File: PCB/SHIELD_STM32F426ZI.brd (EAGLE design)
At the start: 100 x 80 mm, 1 part, among them U1 NUCLEO-F429ZI

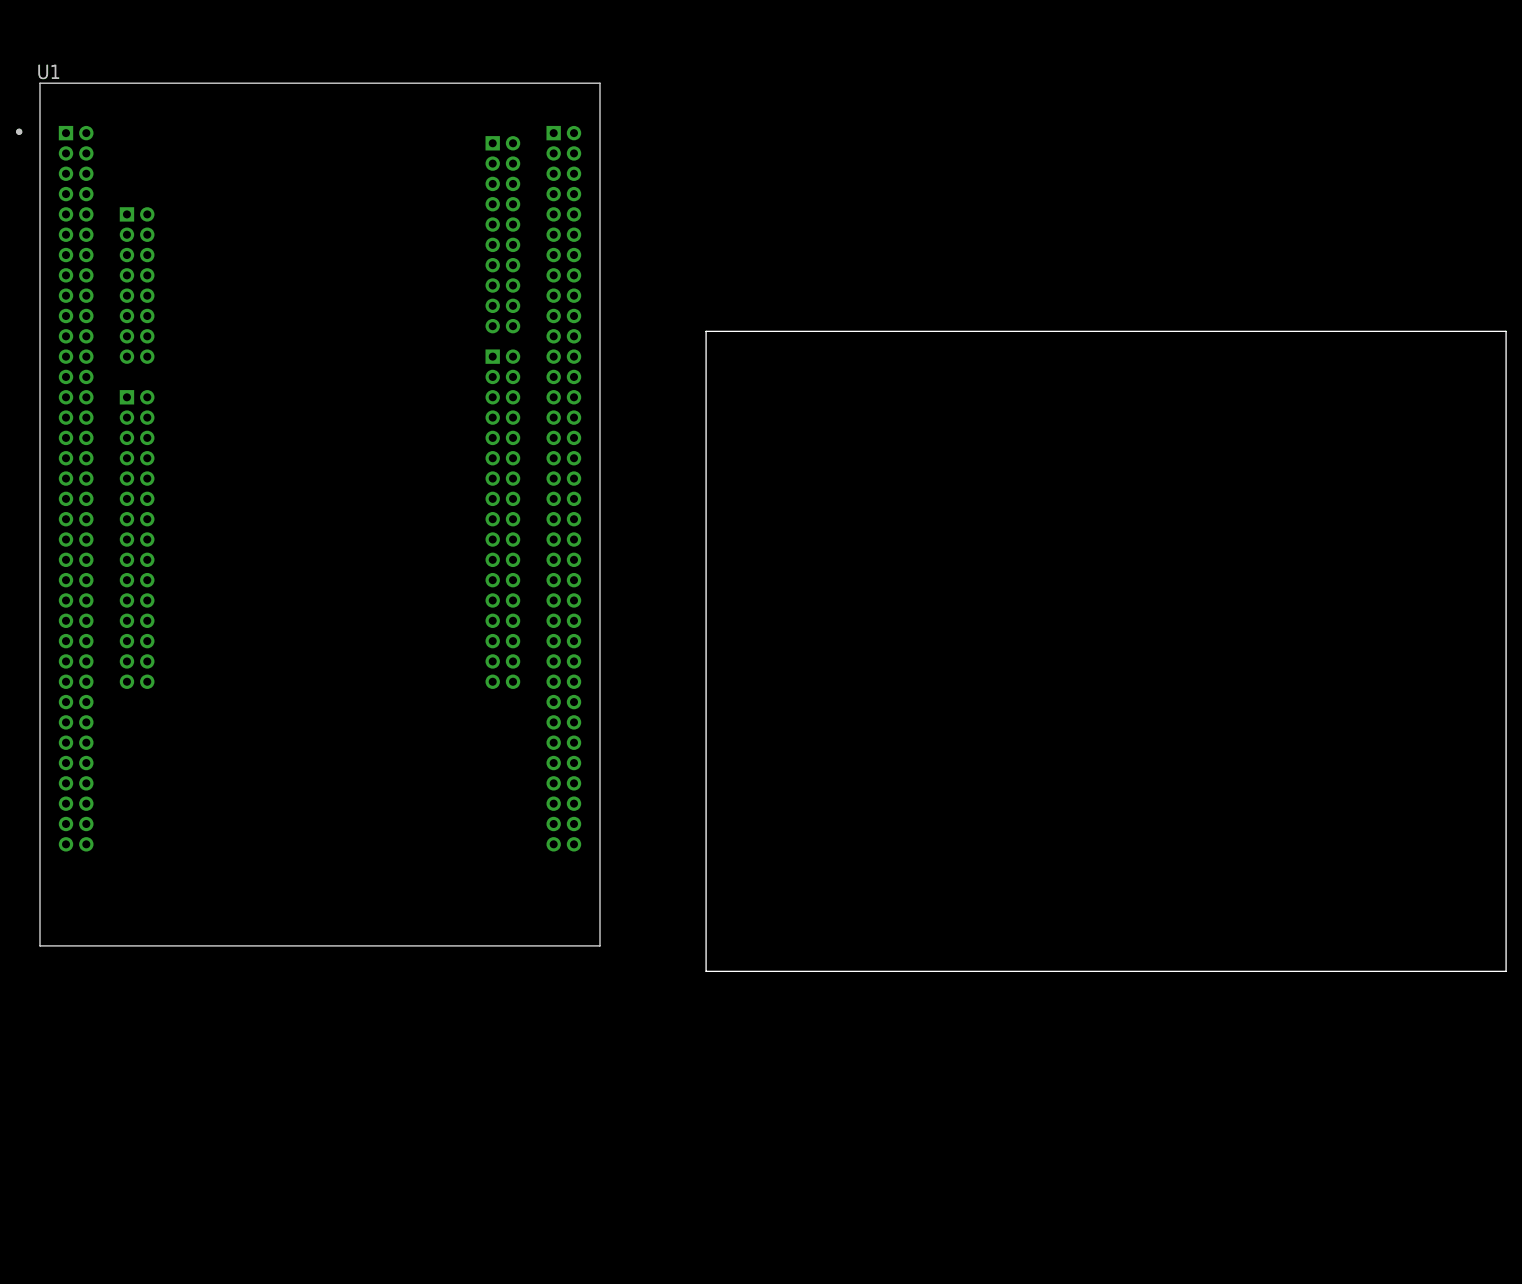
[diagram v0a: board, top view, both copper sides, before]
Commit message: new fmc pin
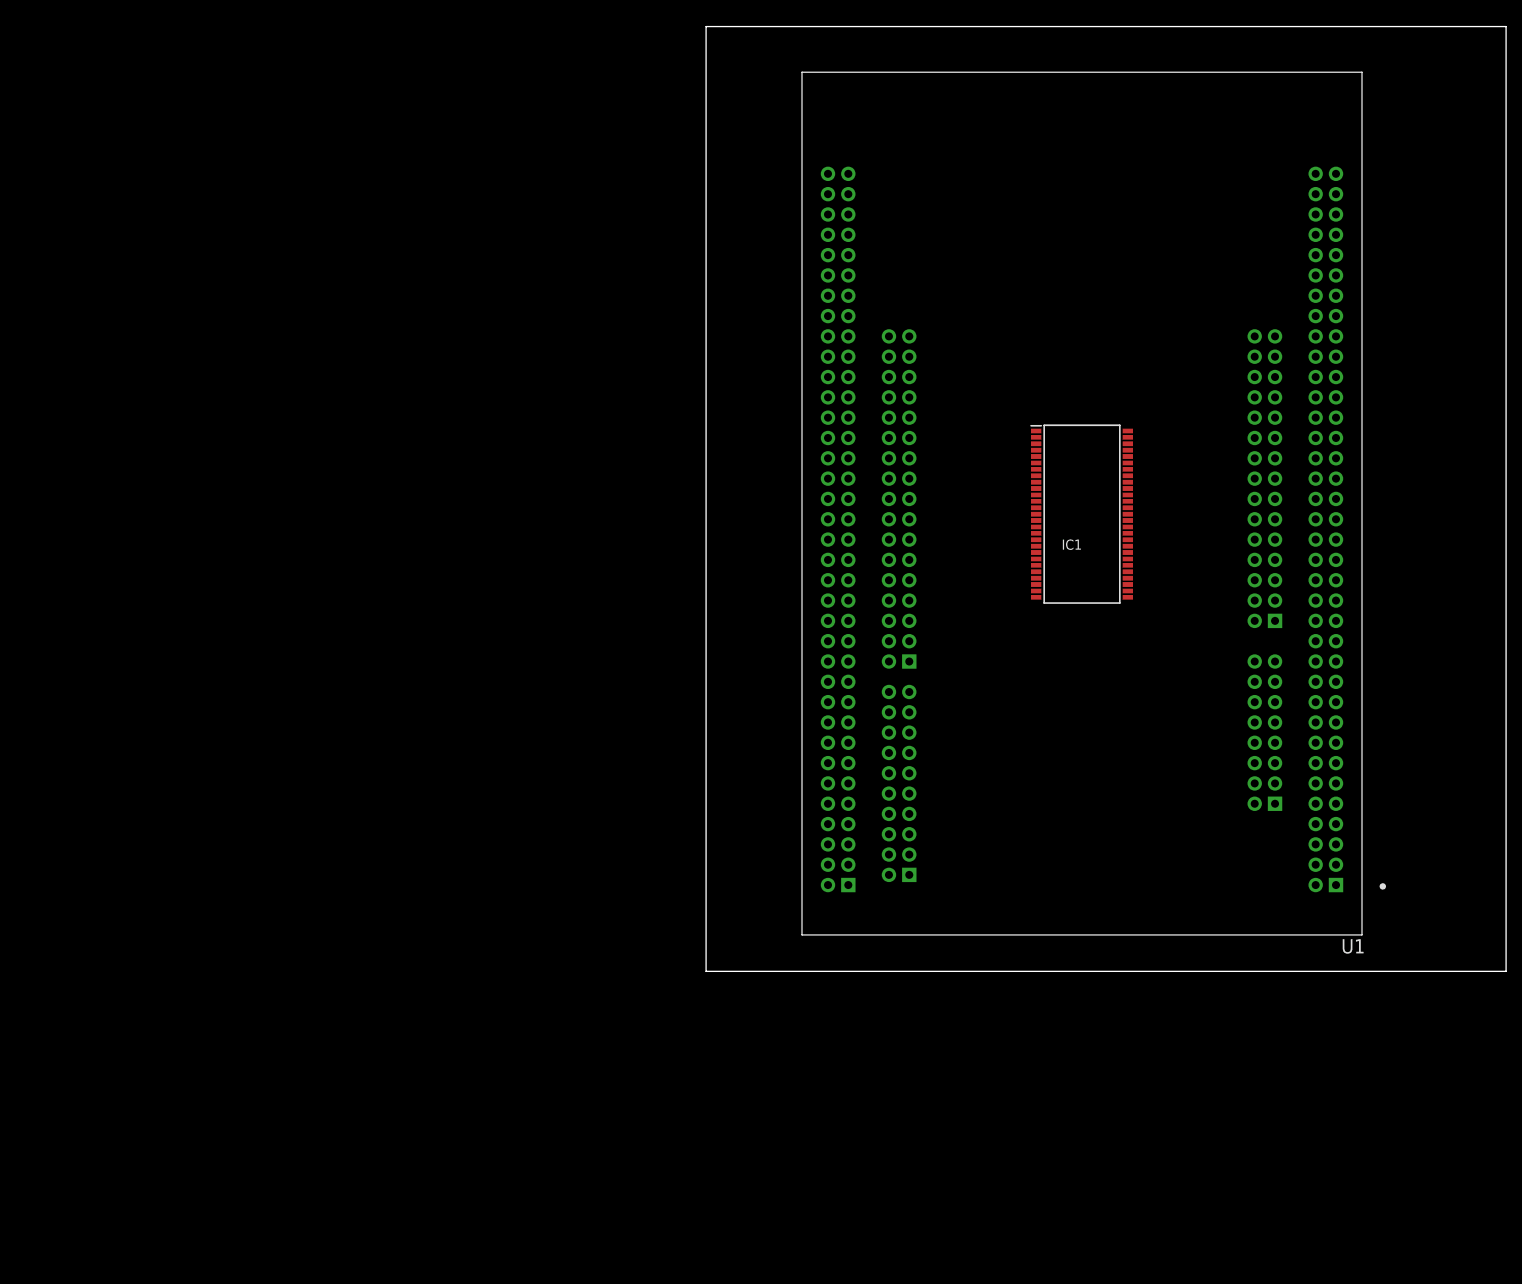
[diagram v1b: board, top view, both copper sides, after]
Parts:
- added IC1: AS4C16M16SA-6TCN, sdram:SOP80P1176X120-54N
- moved U1 95.3 mm to (47.0, 55.9), turned to 180 degrees
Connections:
- new net FMC_A0: IC1.23, U1.CN11_53
- new net FMC_A1: IC1.24, U1.CN11_51
- new net FMC_A10: IC1.22
- new net FMC_A11: IC1.35
- new net FMC_A12: IC1.36
- new net FMC_A2: IC1.25, U1.CN11_52
- new net FMC_A3: IC1.26, U1.CN12_58
- new net FMC_A4: IC1.29, U1.CN12_38
- new net FMC_A5: IC1.30, U1.CN12_36
- new net FMC_A6: IC1.31, U1.CN12_59
- new net FMC_A7: IC1.32, U1.CN12_57
- new net FMC_A8: IC1.33, U1.CN12_50
- new net FMC_A9: IC1.34, U1.CN12_60
- new net N$1: IC1.1
- new net N$10: IC1.10
- new net N$100: U1.CN11_57
- new net N$101: U1.CN11_58
- new net N$102: U1.CN11_59
- new net N$103: U1.CN11_61
- new net N$104: U1.CN11_62
- new net N$105: U1.CN11_63
- new net N$106: U1.CN11_64
- new net N$107: U1.CN11_65
- new net N$108: U1.CN11_66
- new net N$109: U1.CN11_68
- new net N$11: IC1.11
- new net N$110: U1.CN11_69
- new net N$111: U1.CN11_70
- new net N$112: U1.CN12_12
- new net N$113: U1.CN12_13
- new net N$114: U1.CN12_14
- new net N$115: U1.CN12_15
- new net N$116: U1.CN12_16
- new net N$117: U1.CN12_17
- new net N$118: U1.CN12_18
- new net N$119: U1.CN12_19
- new net N$12: IC1.12
- new net N$120: U1.CN12_21
- new net N$121: U1.CN12_22
- new net N$122: U1.CN12_23
- new net N$123: U1.CN12_24
- new net N$124: U1.CN12_25
- new net N$125: U1.CN12_26
- new net N$126: U1.CN12_27
- new net N$127: U1.CN12_28
- new net N$128: U1.CN12_29
- new net N$129: U1.CN12_30
- new net N$13: IC1.13
- new net N$130: U1.CN12_31
- new net N$131: U1.CN12_32
- new net N$132: U1.CN12_33
- new net N$133: U1.CN12_34
- new net N$134: U1.CN12_35
- new net N$136: U1.CN12_37
- new net N$138: U1.CN12_40
- new net N$139: U1.CN12_41
- new net N$14: IC1.14
- new net N$140: U1.CN12_42
- new net N$141: U1.CN12_43
- new net N$142: U1.CN12_44
- new net N$143: U1.CN12_45
- new net N$144: U1.CN12_46
- new net N$145: U1.CN12_47
- new net N$146: U1.CN12_48
- new net N$147: U1.CN12_49
- new net N$149: U1.CN12_51
- new net N$15: IC1.15
- new net N$150: U1.CN12_52
- new net N$151: U1.CN12_53
- new net N$152: U1.CN12_55
- new net N$153: U1.CN12_56
- new net N$158: U1.CN12_61
- new net N$159: U1.CN12_62
- new net N$16: IC1.16
- new net N$160: U1.CN12_64
- new net N$161: U1.CN12_65
- new net N$162: U1.CN12_66
- new net N$163: U1.CN12_67
- new net N$164: U1.CN12_68
- new net N$165: U1.CN12_69
- new net N$166: U1.CN12_70
- new net N$17: IC1.17
- new net N$18: IC1.18
- new net N$19: IC1.19
- new net N$2: IC1.2
- new net N$20: IC1.20
- new net N$21: IC1.21
- new net N$22: U1.CN12_1
- new net N$23: U1.CN11_1
- new net N$24: U1.CN11_2
- new net N$25: U1.CN11_3
- new net N$26: IC1.27
- new net N$27: IC1.54
- new net N$28: IC1.53
- new net N$29: IC1.52
- new net N$3: IC1.3
- new net N$30: IC1.51
- new net N$31: IC1.50
- new net N$32: IC1.49
- new net N$33: IC1.48
- new net N$34: IC1.47
- new net N$35: IC1.46
- new net N$36: IC1.45
- new net N$37: IC1.44
- new net N$38: IC1.43
- new net N$39: IC1.42
- new net N$4: IC1.4
- new net N$40: IC1.41
- new net N$41: IC1.40
- new net N$42: IC1.39
- new net N$43: IC1.38
- new net N$44: IC1.37
- new net N$45: U1.CN12_2
- new net N$46: U1.CN12_3
- new net N$47: U1.CN12_4
- new net N$48: U1.CN12_5
- new net N$49: U1.CN12_6
- new net N$5: IC1.5
- new net N$50: U1.CN12_7
- new net N$51: U1.CN12_8
- new net N$52: U1.CN12_20, U1.CN12_39, U1.CN12_54, U1.CN12_63, U1.CN12_71, U1.CN12_72, U1.CN12_9
- new net N$53: IC1.28
- new net N$54: U1.CN11_4
- new net N$55: U1.CN11_5
- new net N$56: U1.CN11_6
- new net N$57: U1.CN11_7
- new net N$58: U1.CN11_9
- new net N$59: U1.CN11_11
- new net N$6: IC1.6
- new net N$60: U1.CN11_12
- new net N$61: U1.CN11_13
- new net N$62: U1.CN11_14
- new net N$63: U1.CN11_15
- new net N$64: U1.CN11_16
- new net N$65: U1.CN11_17
- new net N$66: U1.CN11_18
- new net N$67: U1.CN11_19, U1.CN11_20, U1.CN11_22, U1.CN11_49, U1.CN11_60, U1.CN11_71, U1.CN11_72, U1.CN11_8
- new net N$68: U1.CN11_21
- new net N$69: U1.CN11_23
- new net N$7: IC1.7
- new net N$70: U1.CN11_24
- new net N$71: U1.CN11_25
- new net N$72: U1.CN11_27
- new net N$73: U1.CN11_28
- new net N$74: U1.CN11_29
- new net N$75: U1.CN11_30
- new net N$76: U1.CN11_31
- new net N$77: U1.CN11_32
- new net N$78: U1.CN11_33
- new net N$79: U1.CN11_34
- new net N$8: IC1.8
- new net N$80: U1.CN11_35
- new net N$81: U1.CN11_36
- new net N$82: U1.CN11_37
- new net N$83: U1.CN11_38
- new net N$84: U1.CN11_39
- new net N$85: U1.CN11_40
- new net N$86: U1.CN11_41
- new net N$87: U1.CN11_42
- new net N$88: U1.CN11_43
- new net N$89: U1.CN11_44
- new net N$9: IC1.9
- new net N$90: U1.CN11_45
- new net N$91: U1.CN11_46
- new net N$92: U1.CN11_47
- new net N$93: U1.CN11_48
- new net N$94: U1.CN11_50
- new net N$95: U1.CN12_10
- new net N$96: U1.CN12_11
- new net N$97: U1.CN11_54
- new net N$98: U1.CN11_55
- new net N$99: U1.CN11_56
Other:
- board size 100 x 80 mm -> 100 x 118.1 mm

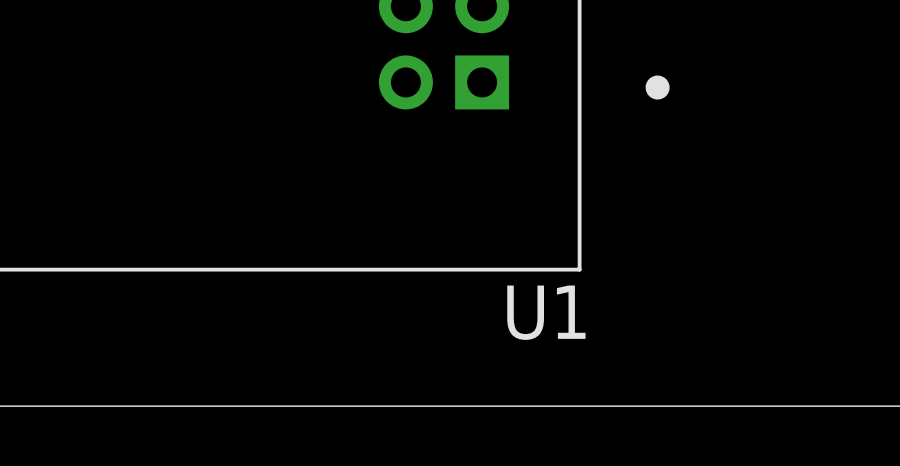
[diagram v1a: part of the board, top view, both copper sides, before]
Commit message: sdram und stm32f4 verdrahten
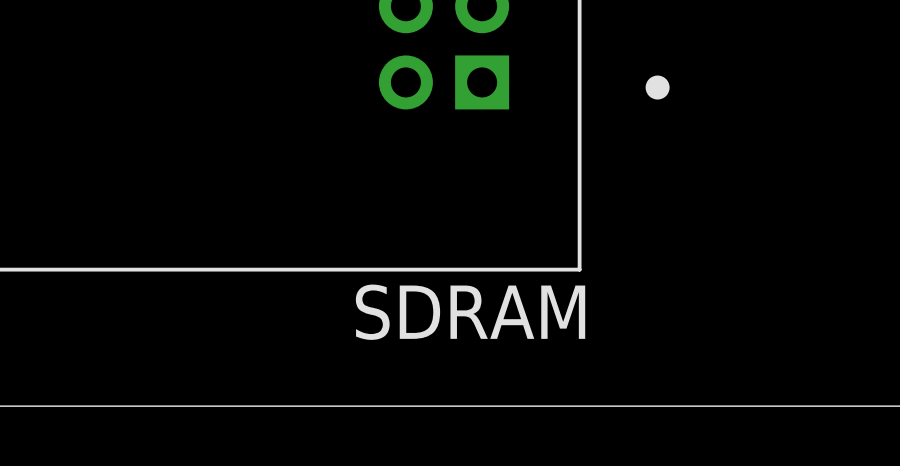
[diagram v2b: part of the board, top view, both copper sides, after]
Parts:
- renumbered U1 to SDRAM
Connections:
- net N$80 renamed FMC_SDNE0
- removed net N$10: IC1.10
- removed net N$100: SDRAM.CN11_57
- removed net N$106: SDRAM.CN11_64
- removed net N$11: IC1.11
- removed net N$110: SDRAM.CN11_69
- removed net N$13: IC1.13
- removed net N$138: SDRAM.CN12_40
- removed net N$142: SDRAM.CN12_44
- removed net N$144: SDRAM.CN12_46
- removed net N$145: SDRAM.CN12_47
- removed net N$146: SDRAM.CN12_48
- removed net N$147: SDRAM.CN12_49
- removed net N$149: SDRAM.CN12_51
- removed net N$150: SDRAM.CN12_52
- removed net N$151: SDRAM.CN12_53
- removed net N$152: SDRAM.CN12_55
- removed net N$153: SDRAM.CN12_56
- removed net N$159: SDRAM.CN12_62
- removed net N$16: IC1.16
- removed net N$161: SDRAM.CN12_65
- removed net N$162: SDRAM.CN12_66
- removed net N$164: SDRAM.CN12_68
- removed net N$165: SDRAM.CN12_69
- removed net N$17: IC1.17
- removed net N$18: IC1.18
- removed net N$2: IC1.2
- removed net N$20: IC1.20
- removed net N$21: IC1.21
- removed net N$28: IC1.53
- removed net N$30: IC1.51
- removed net N$31: IC1.50
- removed net N$33: IC1.48
- removed net N$34: IC1.47
- removed net N$36: IC1.45
- removed net N$37: IC1.44
- removed net N$39: IC1.42
- removed net N$4: IC1.4
- removed net N$43: IC1.38
- removed net N$44: IC1.37
- removed net N$5: IC1.5
- removed net N$7: IC1.7
- removed net N$8: IC1.8
- removed net N$82: SDRAM.CN11_37
- removed net N$83: SDRAM.CN11_38
- removed net N$95: SDRAM.CN12_10
- removed net N$98: SDRAM.CN11_55
- new net FMC_BA0: IC1.20, SDRAM.CN12_69
- new net FMC_BA1: IC1.21, SDRAM.CN12_68
- new net FMC_D0: IC1.2, SDRAM.CN12_46
- new net FMC_D1: IC1.4, SDRAM.CN12_48
- new net FMC_D10: IC1.45, SDRAM.CN12_55
- new net FMC_D11: IC1.47, SDRAM.CN12_51
- new net FMC_D12: IC1.48, SDRAM.CN12_53
- new net FMC_D13: IC1.50, SDRAM.CN12_10
- new net FMC_D14: IC1.51, SDRAM.CN11_69
- new net FMC_D15: IC1.53, SDRAM.CN12_65
- new net FMC_D2: IC1.5, SDRAM.CN11_57
- new net FMC_D3: IC1.7, SDRAM.CN11_55
- new net FMC_D4: IC1.8, SDRAM.CN12_44
- new net FMC_D5: IC1.10, SDRAM.CN12_40
- new net FMC_D6: IC1.11, SDRAM.CN12_52
- new net FMC_D7: IC1.13, SDRAM.CN12_47
- new net FMC_D8: IC1.42, SDRAM.CN12_56
- new net FMC_D9: IC1.44, SDRAM.CN12_49
- new net FMC_SDCKE0: IC1.37, SDRAM.CN11_37
- new net FMC_SDCLK: IC1.38, SDRAM.CN12_66
- new net FMC_SDNCAS: IC1.17, SDRAM.CN11_64
- new net FMC_SDNRAS: IC1.18, SDRAM.CN12_62
- new net FMC_SDNWE: IC1.16, SDRAM.CN11_38
